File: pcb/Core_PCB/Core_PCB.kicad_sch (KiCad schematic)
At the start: 0 parts

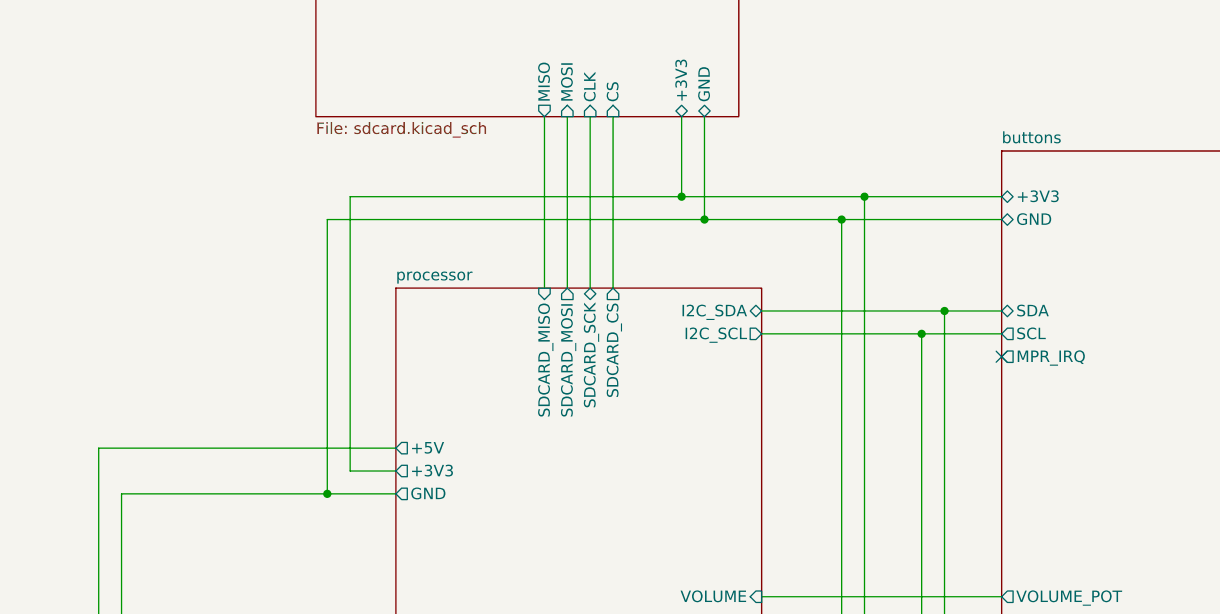
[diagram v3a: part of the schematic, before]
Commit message: SCH - audio: screw terminal was facing the wrong direction; buttons: volume pot had wrong footprint, added +5V input; processor: use alternative arduino symbol and custom footprint (with 3d model), added reset switch, adjusted rule for PWR lines
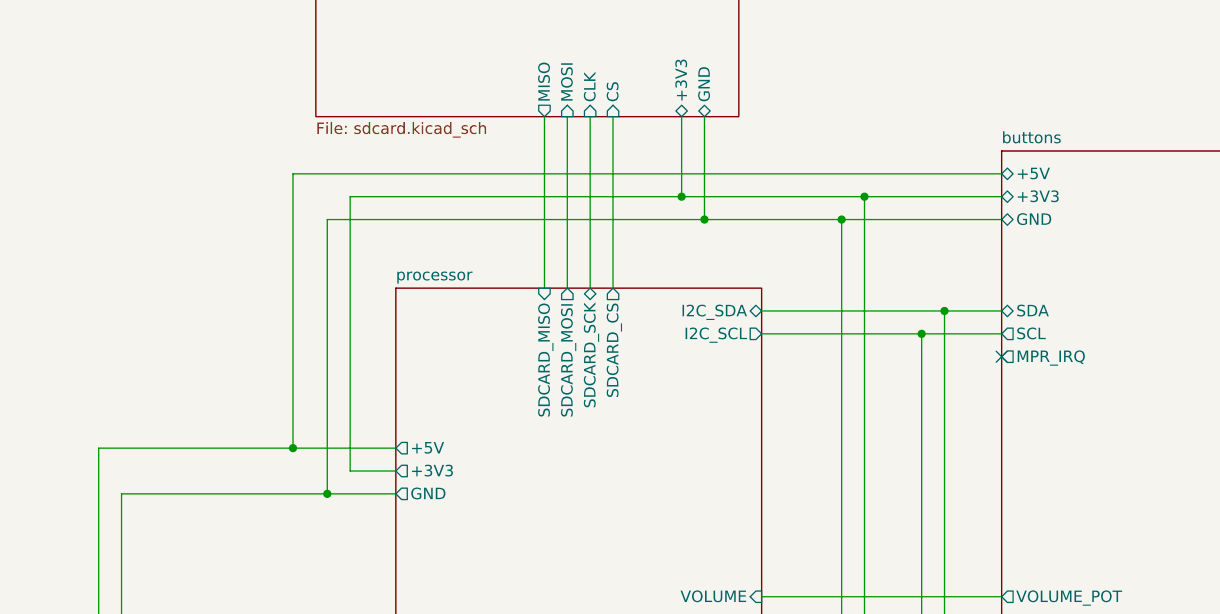
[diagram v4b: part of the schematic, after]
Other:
- sheet buttons ports: added +5V; removed none
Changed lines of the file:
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@@
+	)
+	(junction
+		(at 92.71 81.28)
+		(diameter 0)
+		(color 0 0 0 0)
 	)
 	(junction
@@
 	(wire
 		(pts
-			(xy 71.12 81.28) (xy 104.14 81.28)
+			(xy 71.12 81.28) (xy 92.71 81.28)
 		)
 		(stroke
@@
 	(wire
 		(pts
+			(xy 92.71 81.28) (xy 104.14 81.28)
+		)
+		(stroke
+			(width 0)
+			(type default)
+		)
+	)
+	(wire
+		(pts
 			(xy 144.78 97.79) (xy 171.45 97.79)
 		)
@@
 	(wire
 		(pts
+			(xy 92.71 50.8) (xy 92.71 81.28)
+		)
+		(stroke
+			(width 0)
+			(type default)
+		)
+	)
+	(wire
+		(pts
 			(xy 165.1 66.04) (xy 171.45 66.04)
+		)
+		(stroke
+			(width 0)
+			(type default)
+		)
+	)
+	(wire
+		(pts
+			(xy 171.45 50.8) (xy 92.71 50.8)
 		)
 		(stroke
@@
 			(effects
 				(font
+					(size 1.27 1.27)
+				)
+				(justify left)
+			)
+		)
+		(pin "+5V" bidirectional
+			(at 171.45 50.8 180)
+			(effects
+				(font

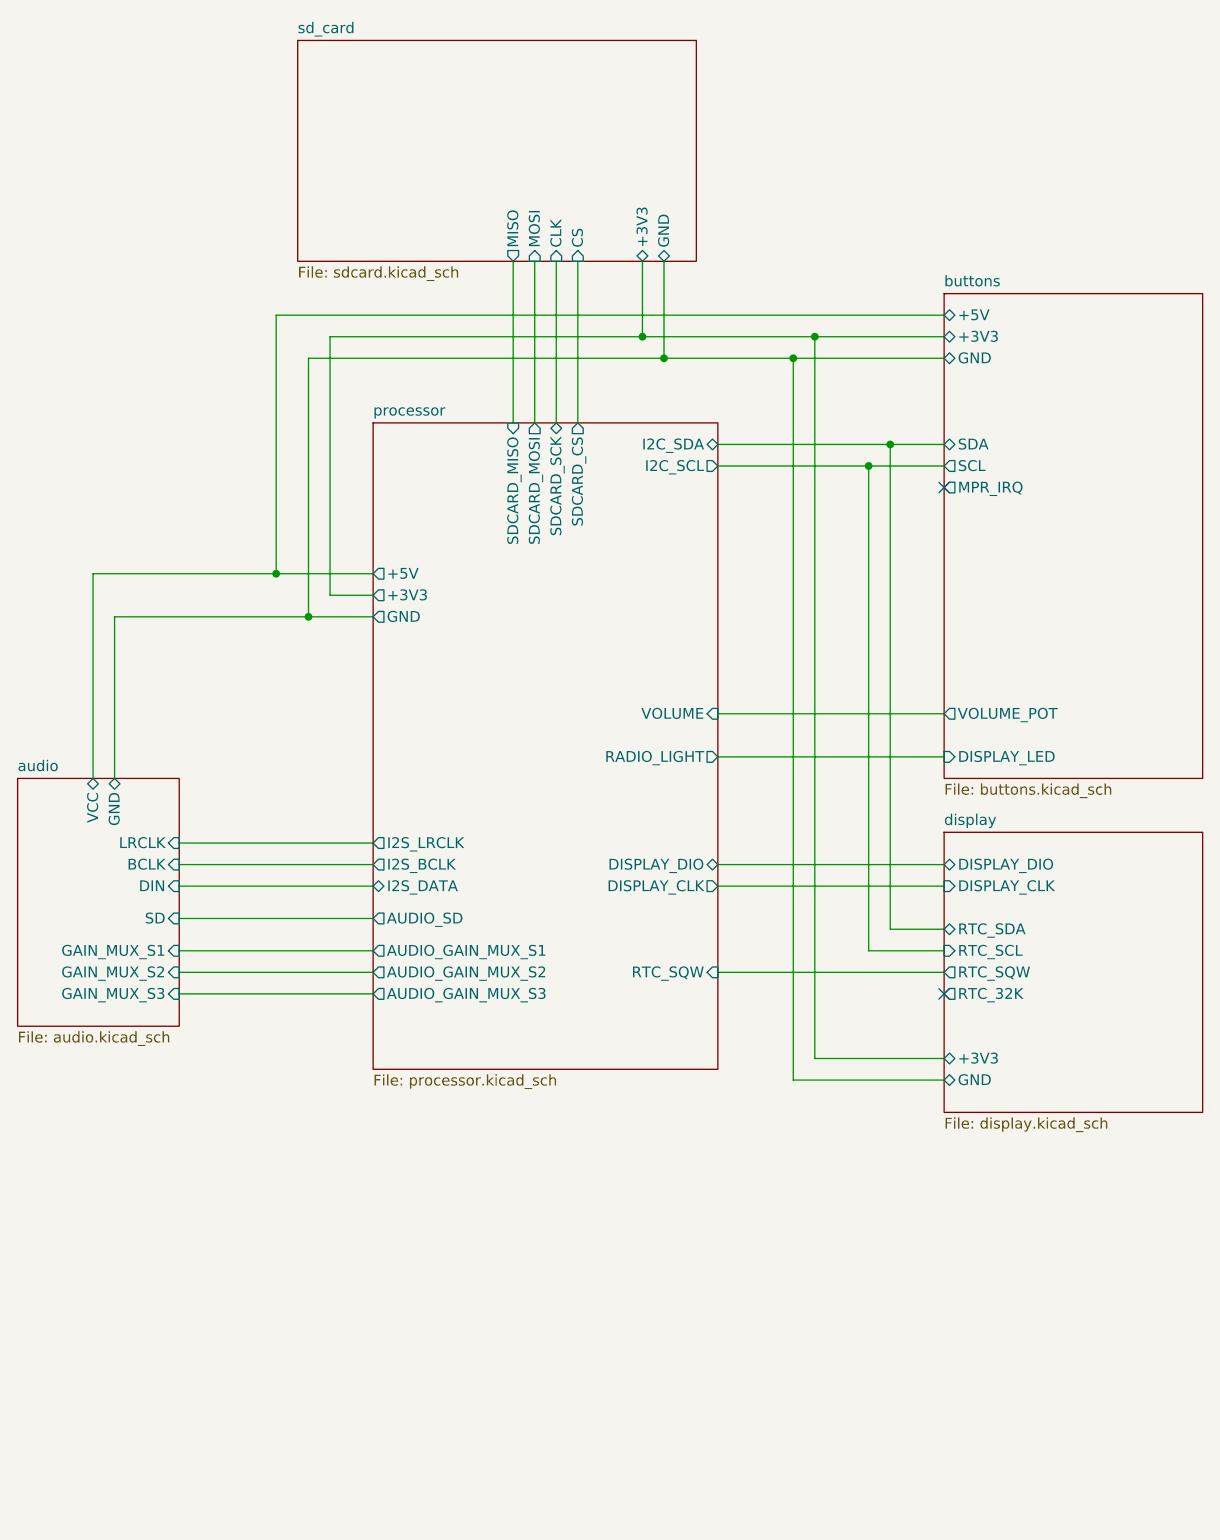
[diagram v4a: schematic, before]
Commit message: use a potentiometer connector (picoblade) and moved it to the audio sch; touch interface (capacitance measureer) got a 2 row connector with GND on one line; added mounting screws and logo to the main sch (and lib)
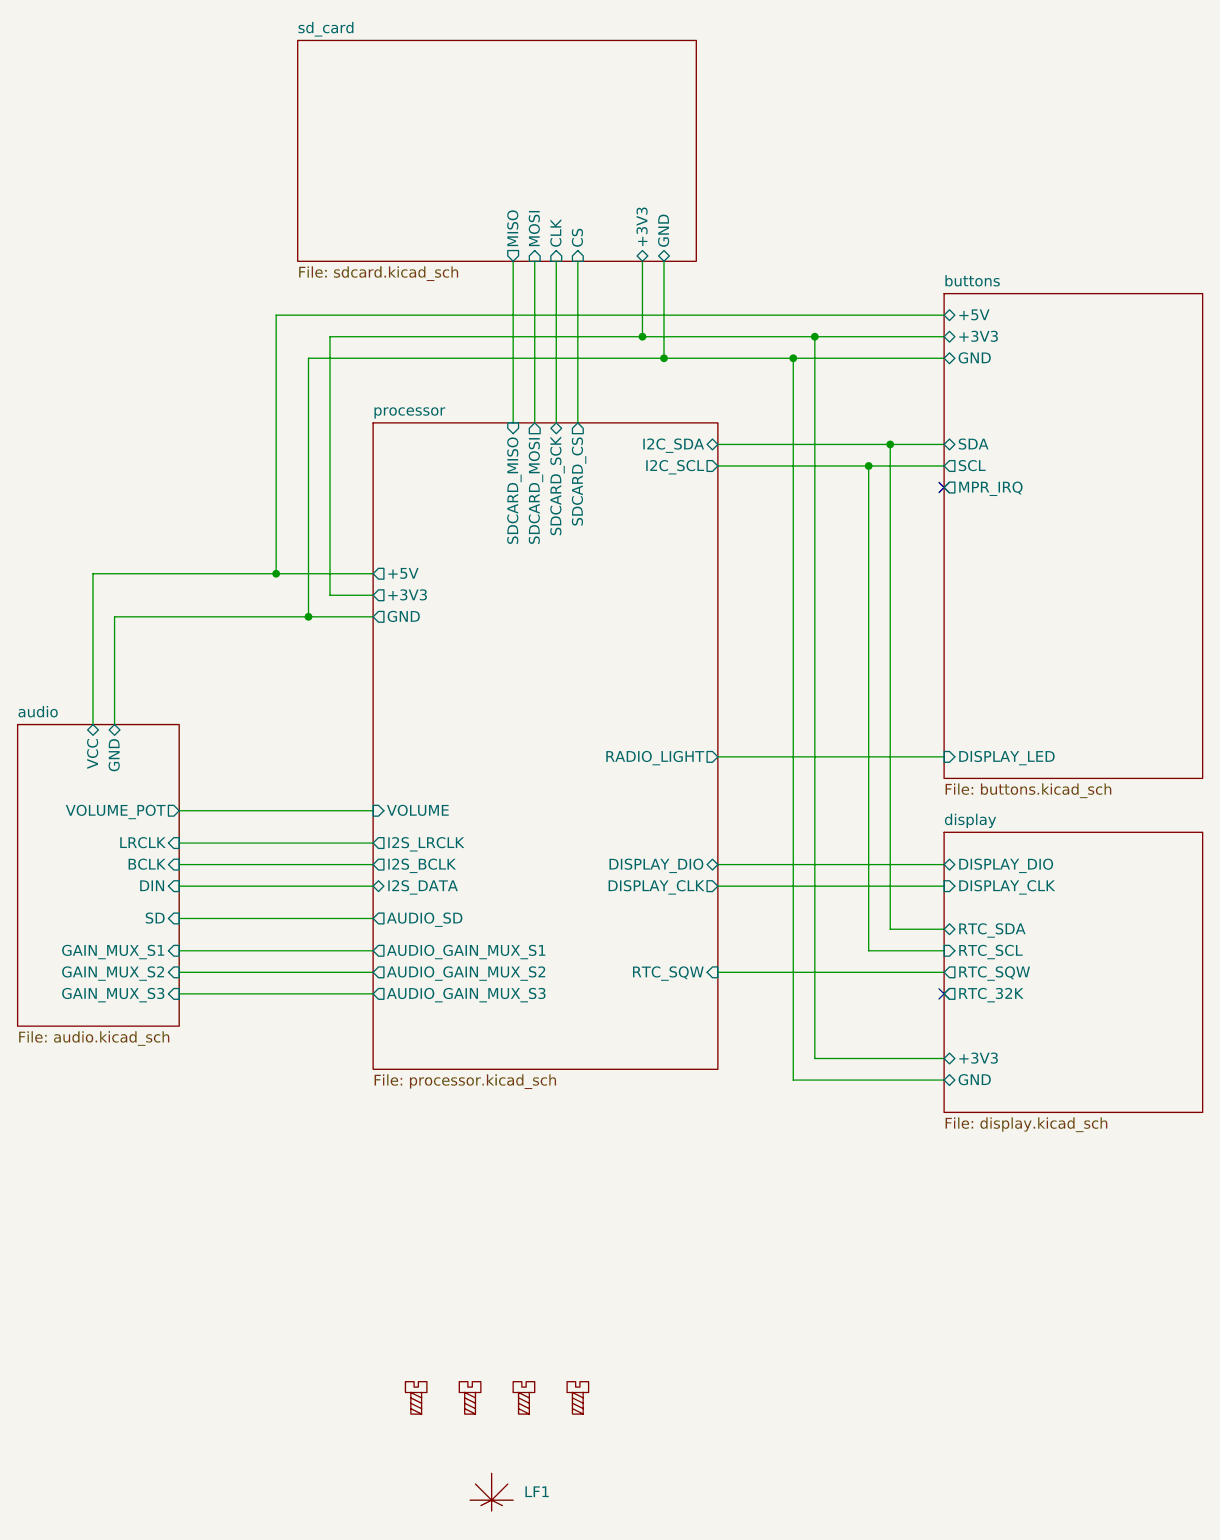
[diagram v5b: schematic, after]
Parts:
- added H1, H2, H3, H4: MountingScrew, MountingHole:MountingHole_3.2mm_M3, symbol Auxiliary_Items:MountingScrew
- added LF1: (no value), RadioWecker:LEAF, symbol RadioWecker:LEAF
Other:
- sheet audio ports: added VOLUME_POT; removed none
- sheet buttons ports: added none; removed VOLUME_POT

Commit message: SCH: audio - forgot the +3V3 hierarchical label, renamed VCC to +5V, made screw terminal not populated (use the one on the i2s module) SCH general: bumped date
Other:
- sheet audio ports: added +3V3, +5V; removed VCC
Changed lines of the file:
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@@
 	(title_block
 		(title "Alarm Clock Resto Mod - Core PCB")
-		(date "2026-07-08")
+		(date "2026-07-28")
 		(rev "1.0")
 		(company "brunolalb@gmail.com")
@@
 	)
 	(junction
+		(at 99.06 83.82)
+		(diameter 0)
+		(color 0 0 0 0)
+	)
+	(junction
 		(at 162.56 68.58)
 		(diameter 0)
@@
 	(wire
 		(pts
-			(xy 71.12 81.28) (xy 92.71 81.28)
+			(xy 68.58 81.28) (xy 92.71 81.28)
 		)
 		(stroke
@@
 	(wire
 		(pts
+			(xy 99.06 83.82) (xy 71.12 83.82)
+		)
+		(stroke
+			(width 0)
+			(type default)
+		)
+	)
+	(wire
+		(pts
 			(xy 123.19 44.45) (xy 123.19 63.5)
 		)
@@
 	(wire
 		(pts
+			(xy 71.12 83.82) (xy 71.12 99.06)
+		)
+		(stroke
+			(width 0)
+			(type default)
+		)
+	)
+	(wire
+		(pts
 			(xy 135.89 44.45) (xy 135.89 53.34)
 		)
@@
 	(wire
 		(pts
-			(xy 71.12 99.06) (xy 71.12 81.28)
+			(xy 68.58 99.06) (xy 68.58 81.28)
 		)
 		(stroke
@@
 			)
 		)
+		(pin "LRCLK" input
+			(at 81.28 113.03 0)
+			(effects
+				(font
+					(size 1.27 1.27)
+				)
+				(justify right)
+			)
+		)
+		(pin "DIN" input
+			(at 81.28 118.11 0)
+			(effects
+				(font
+					(size 1.27 1.27)
+				)
+				(justify right)
+			)
+		)
+		(pin "SD" input
+			(at 81.28 121.92 0)
+			(effects
+				(font
+					(size 1.27 1.27)
+				)
+				(justify right)
+			)
+		)
+		(pin "BCLK" input
+			(at 81.28 115.57 0)
+			(effects
+				(font
+					(size 1.27 1.27)
+				)
+				(justify right)
+			)
+		)
+		(pin "GAIN_MUX_S1" input
+			(at 81.28 125.73 0)
+			(effects
+				(font
+					(size 1.27 1.27)
+				)
+				(justify right)
+			)
+		)
+		(pin "GAIN_MUX_S2" input
+			(at 81.28 128.27 0)
+			(effects
+				(font
+					(size 1.27 1.27)
+				)
+				(justify right)
+			)
+		)
+		(pin "GAIN_MUX_S3" input
+			(at 81.28 130.81 0)
+			(effects
+				(font
+					(size 1.27 1.27)
+				)
+				(justify right)
+			)
+		)
+		(pin "VOLUME_POT" output
+			(at 81.28 109.22 0)
+			(effects
+				(font
+					(size 1.27 1.27)
+				)
+				(justify right)
+			)
+		)
+		(pin "+5V" bidirectional
+			(at 68.58 99.06 90)
+			(effects
+				(font
+					(size 1.27 1.27)
+				)
+				(justify right)
+			)
+		)
 		(pin "GND" bidirectional
 			(at 73.66 99.06 90)
@@
 			)
 		)
-		(pin "LRCLK" input
-			(at 81.28 113.03 0)
-			(effects
-				(font
-					(size 1.27 1.27)
-				)
-				(justify right)
-			)
-		)
-		(pin "DIN" input
-			(at 81.28 118.11 0)
-			(effects
-				(font
-					(size 1.27 1.27)
-				)
-				(justify right)
-			)
-		)
-		(pin "VCC" bidirectional
+		(pin "+3V3" bidirectional
 			(at 71.12 99.06 90)
 			(effects
 				(font
-					(size 1.27 1.27)
-				)
-				(justify right)
-			)
-		)
-		(pin "SD" input
-			(at 81.28 121.92 0)
-			(effects
-				(font
-					(size 1.27 1.27)
-				)
-				(justify right)
-			)
-		)
-		(pin "BCLK" input
-			(at 81.28 115.57 0)
-			(effects
-				(font
-					(size 1.27 1.27)
-				)
-				(justify right)
-			)
-		)
-		(pin "GAIN_MUX_S1" input
-			(at 81.28 125.73 0)
-			(effects
-				(font
-					(size 1.27 1.27)
-				)
-				(justify right)
-			)
-		)
-		(pin "GAIN_MUX_S2" input
-			(at 81.28 128.27 0)
-			(effects
-				(font
-					(size 1.27 1.27)
-				)
-				(justify right)
-			)
-		)
-		(pin "GAIN_MUX_S3" input
-			(at 81.28 130.81 0)
-			(effects
-				(font
-					(size 1.27 1.27)
-				)
-				(justify right)
-			)
-		)
-		(pin "VOLUME_POT" output
-			(at 81.28 109.22 0)
-			(effects
-				(font

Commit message: PCBs: updated logo; added I2C resistors to I2C (core pcb)
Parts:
- removed LF1: (no value), RadioWecker:LEAF, symbol RadioWecker:LEAF
- added G1: LOGO, RadioWecker:LOGO, symbol RadioWecker:LOGO
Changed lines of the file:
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@@
+	)
+	(symbol
+		(lib_id "RadioWecker:LOGO")
+		(at 118.11 189.23 0)
+		(unit 1)
+		(body_style 1)
+		(exclude_from_sim no)
+		(in_bom no)
+		(on_board yes)
+		(in_pos_files yes)
+		(dnp no)
+		(fields_autoplaced yes)
+		(property "Reference" "G1"
+			(at 118.11 184.8648 0)
+			(hide yes)
+			(show_name no)
+			(do_not_autoplace no)
+			(effects
+				(font
+					(size 1.27 1.27)
+				)
+			)
+		)
+		(property "Value" "LOGO"
+			(at 118.11 193.5952 0)
+			(hide yes)
+			(show_name no)
+			(do_not_autoplace no)
+			(effects
+				(font
+					(size 1.27 1.27)
+				)
+			)
+		)
+		(property "Footprint" "RadioWecker:LOGO"
+			(at 118.364 195.58 0)
+			(hide yes)
+			(show_name no)
+			(do_not_autoplace no)
+			(effects
+				(font
+					(size 1.27 1.27)
+				)
+			)
+		)
+		(property "Datasheet" ""
+			(at 118.11 189.23 0)
+			(hide yes)
+			(show_name no)
+			(do_not_autoplace no)
+			(effects
+				(font
+					(size 1.27 1.27)
+				)
+			)
+		)
+		(property "Description" ""
+			(at 118.11 189.23 0)
+			(hide yes)
+			(show_name no)
+			(do_not_autoplace no)
+			(effects
+				(font
+					(size 1.27 1.27)
+				)
+			)
+		)
+		(instances
+			(project "Core_PCB"
+				(path "/79975d02-cfea-4cc3-8869-9743c86248b2"
+					(reference "G1")
+					(unit 1)
+				)
+			)
+		)
 	)
 	(symbol
@@
 					(unit 1)
 				)
-			)
-		)
-	)
-	(symbol
-		(lib_id "RadioWecker:LEAF")
-		(at 118.11 191.77 0)
-		(unit 1)
-		(body_style 1)
-		(exclude_from_sim no)
-		(in_bom yes)
-		(on_board yes)
-		(in_pos_files yes)
-		(dnp no)
-		(fields_autoplaced yes)
-		(property "Reference" "LF1"
-			(at 121.92 189.5474 0)
-			(show_name no)
-			(do_not_autoplace no)
-			(effects
-				(font
-					(size 1.27 1.27)
-				)
-				(justify left)
-			)
-		)
-		(property "Value" ""
-			(at 118.11 191.77 0)
-			(hide yes)
-			(show_name no)
-			(do_not_autoplace no)
-			(effects
-				(font
-					(size 1.27 1.27)
-				)
-			)
-		)
-		(property "Footprint" "RadioWecker:LEAF"
-			(at 118.364 195.072 0)
-			(hide yes)
-			(show_name no)
-			(do_not_autoplace no)
-			(effects
-				(font
-					(size 1.27 1.27)
-				)
-			)
-		)
-		(property "Datasheet" ""
-			(at 118.11 191.77 0)
-			(hide yes)
-			(show_name no)
-			(do_not_autoplace no)
-			(effects
-				(font
-					(size 1.27 1.27)
-				)
-			)
-		)
-		(property "Description" ""
-			(at 118.11 191.77 0)
-			(hide yes)
-			(show_name no)
-			(do_not_autoplace no)
-			(effects
-				(font
-					(size 1.27 1.27)
-				)
-			)
-		)
-		(instances
-			(project "Core_PCB"
-				(path "/79975d02-cfea-4cc3-8869-9743c86248b2"
-					(reference "LF1")
-					(unit 1)
-				)
